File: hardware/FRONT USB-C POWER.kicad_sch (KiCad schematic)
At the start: 36 parts, among them Q3 PMPB11EN,115, Q4 PMPB11EN,115, Q5 PMPB11EN,115, Q6 PMPB11EN,115

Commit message: messing arround with pcb to finalise
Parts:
- added TP10, TP11: TestPoint, TestPoint:TestPoint_Pad_D1.5mm, symbol Connector:TestPoint
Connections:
- net B_USB-C_BUCK_OUT: now also TP10.1
- net F_USB-C_BUCK_OUT: now also TP11.1
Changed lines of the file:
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@@
   (junction (at 198.12 114.3) (diameter 0) (color 0 0 0 0)
   )
+  (junction (at 41.91 72.39) (diameter 0) (color 0 0 0 0)
+  )
   (junction (at 215.9 73.66) (diameter 0) (color 0 0 0 0)
   )
@@
   (junction (at 138.43 25.4) (diameter 0) (color 0 0 0 0)
   )
+  (junction (at 233.68 73.66) (diameter 0) (color 0 0 0 0)
+  )
   (junction (at 241.3 114.3) (diameter 0) (color 0 0 0 0)
   )
@@
     (stroke (width 0) (type default))
   )
+  (wire (pts (xy 41.91 72.39) (xy 44.45 72.39))
+    (stroke (width 0) (type default))
+  )
   (wire (pts (xy 215.9 73.66) (xy 219.71 73.66))
     (stroke (width 0) (type default))
@@
     (stroke (width 0) (type default))
   )
-  (wire (pts (xy 39.37 72.39) (xy 44.45 72.39))
-    (stroke (width 0) (type default))
-  )
-  (wire (pts (xy 228.6 73.66) (xy 237.49 73.66))
+  (wire (pts (xy 39.37 72.39) (xy 41.91 72.39))
+    (stroke (width 0) (type default))
+  )
+  (wire (pts (xy 228.6 73.66) (xy 233.68 73.66))
     (stroke (width 0) (type default))
   )
@@
   )
   (wire (pts (xy 104.14 87.63) (xy 96.52 87.63))
+    (stroke (width 0) (type default))
+  )
+  (wire (pts (xy 233.68 73.66) (xy 237.49 73.66))
     (stroke (width 0) (type default))
   )
@@
     )
   )
+  (symbol (lib_id "Connector:TestPoint") (at 41.91 72.39 0) (unit 1)
+    (in_bom yes) (on_board yes) (dnp no) (fields_autoplaced)
+    (property "Reference" "TP10" (at 43.307 68.4443 0)
+      (effects (font (size 1.27 1.27)) (justify left))
+    )
+    (property "Value" "TestPoint" (at 43.307 70.3653 0)
+      (effects (font (size 1.27 1.27)) (justify left))
+    )
+    (property "Footprint" "TestPoint:TestPoint_Pad_D1.5mm" (at 46.99 72.39 0)
+      (effects (font (size 1.27 1.27)) hide)
+    )
+    (property "Datasheet" "~" (at 46.99 72.39 0)
+      (effects (font (size 1.27 1.27)) hide)
+    )
+    (pin "1")
+    (instances
+      (project "usbc-car-module"
+        (path "/fae025e9-99c5-40c1-af6f-99dc1edbfa43/91b561d6-4186-4f6f-8a2c-57c2c305f210"
+          (reference "TP10") (unit 1)
+        )
+      )
+    )
+  )
   (symbol (lib_id "Device:C") (at 138.43 143.51 90) (unit 1)
     (in_bom yes) (on_board yes) (dnp no) (fields_autoplaced)
@@
         )
       )
+    )
+  )
+  (symbol (lib_id "Connector:TestPoint") (at 233.68 73.66 0) (unit 1)
+    (in_bom yes) (on_board yes) (dnp no) (fields_autoplaced)
+    (property "Reference" "TP11" (at 235.077 69.7143 0)
+      (effects (font (size 1.27 1.27)) (justify left))
+    )
+    (property "Value" "TestPoint" (at 235.077 71.6353 0)
+      (effects (font (size 1.27 1.27)) (justify left))
+    )
+    (property "Footprint" "TestPoint:TestPoint_Pad_D1.5mm" (at 238.76 73.66 0)
+      (effects (font (size 1.27 1.27)) hide)
+    )
+    (property "Datasheet" "~" (at 238.76 73.66 0)
+      (effects (font (size 1.27 1.27)) hide)
+    )
+    (pin "1")
+    (instances
+      (project "usbc-car-module"
+        (path "/fae025e9-99c5-40c1-af6f-99dc1edbfa43/91b561d6-4186-4f6f-8a2c-57c2c305f210"
+          (reference "TP11") (unit 1)
+        )
+      )

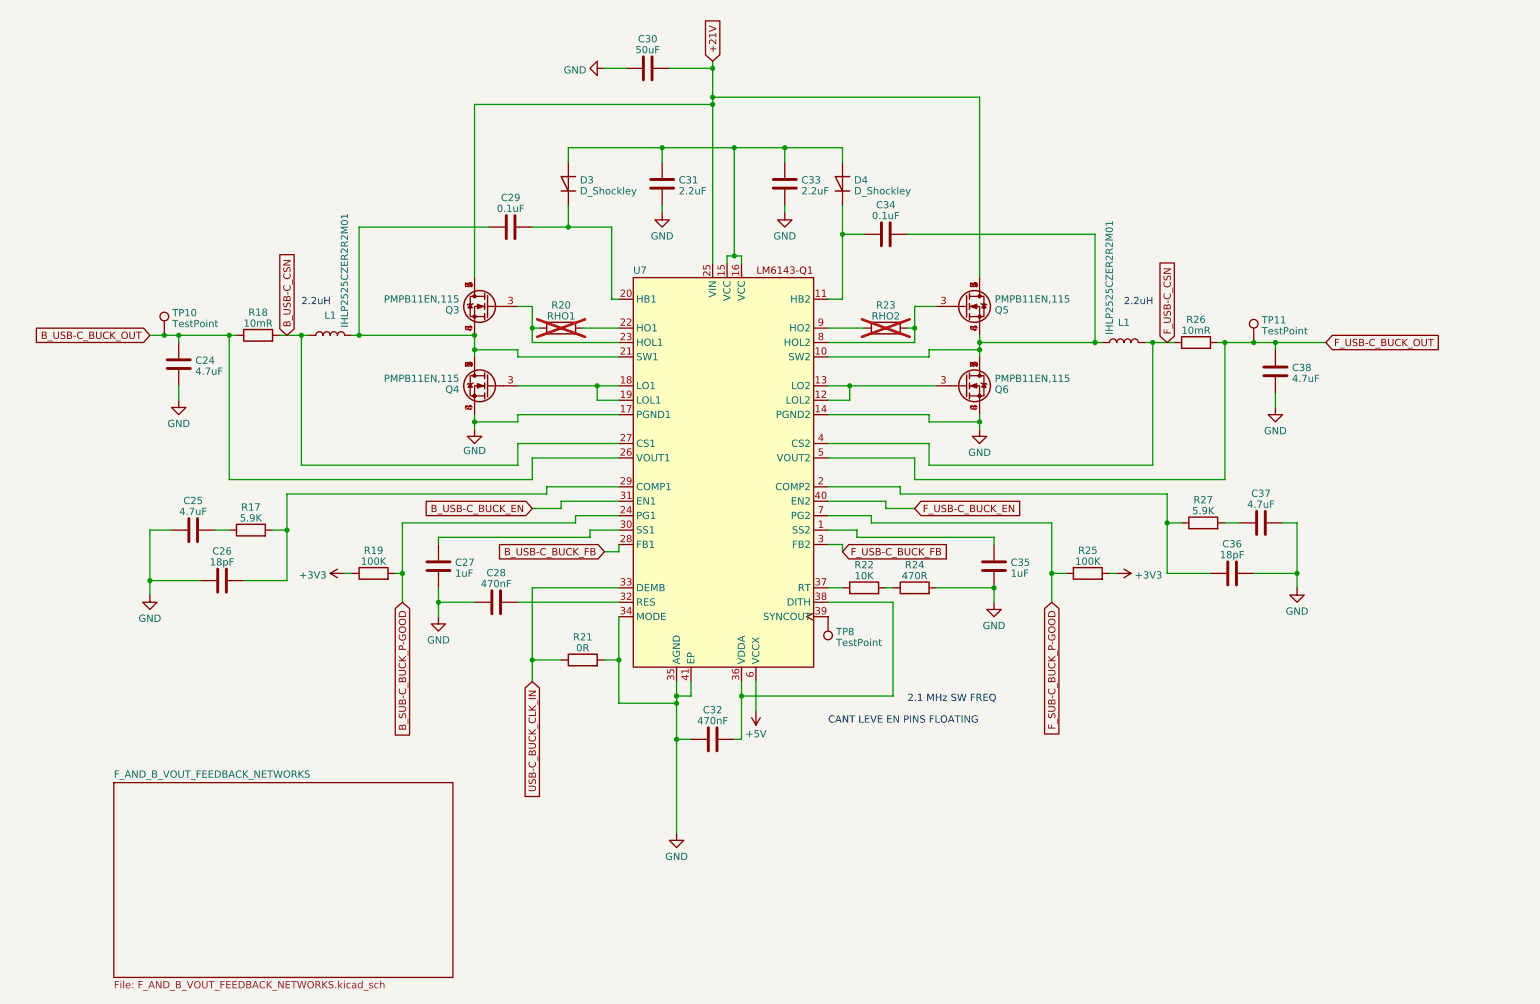
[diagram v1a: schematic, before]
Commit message: fixed DP issues and finneshed overall routeing
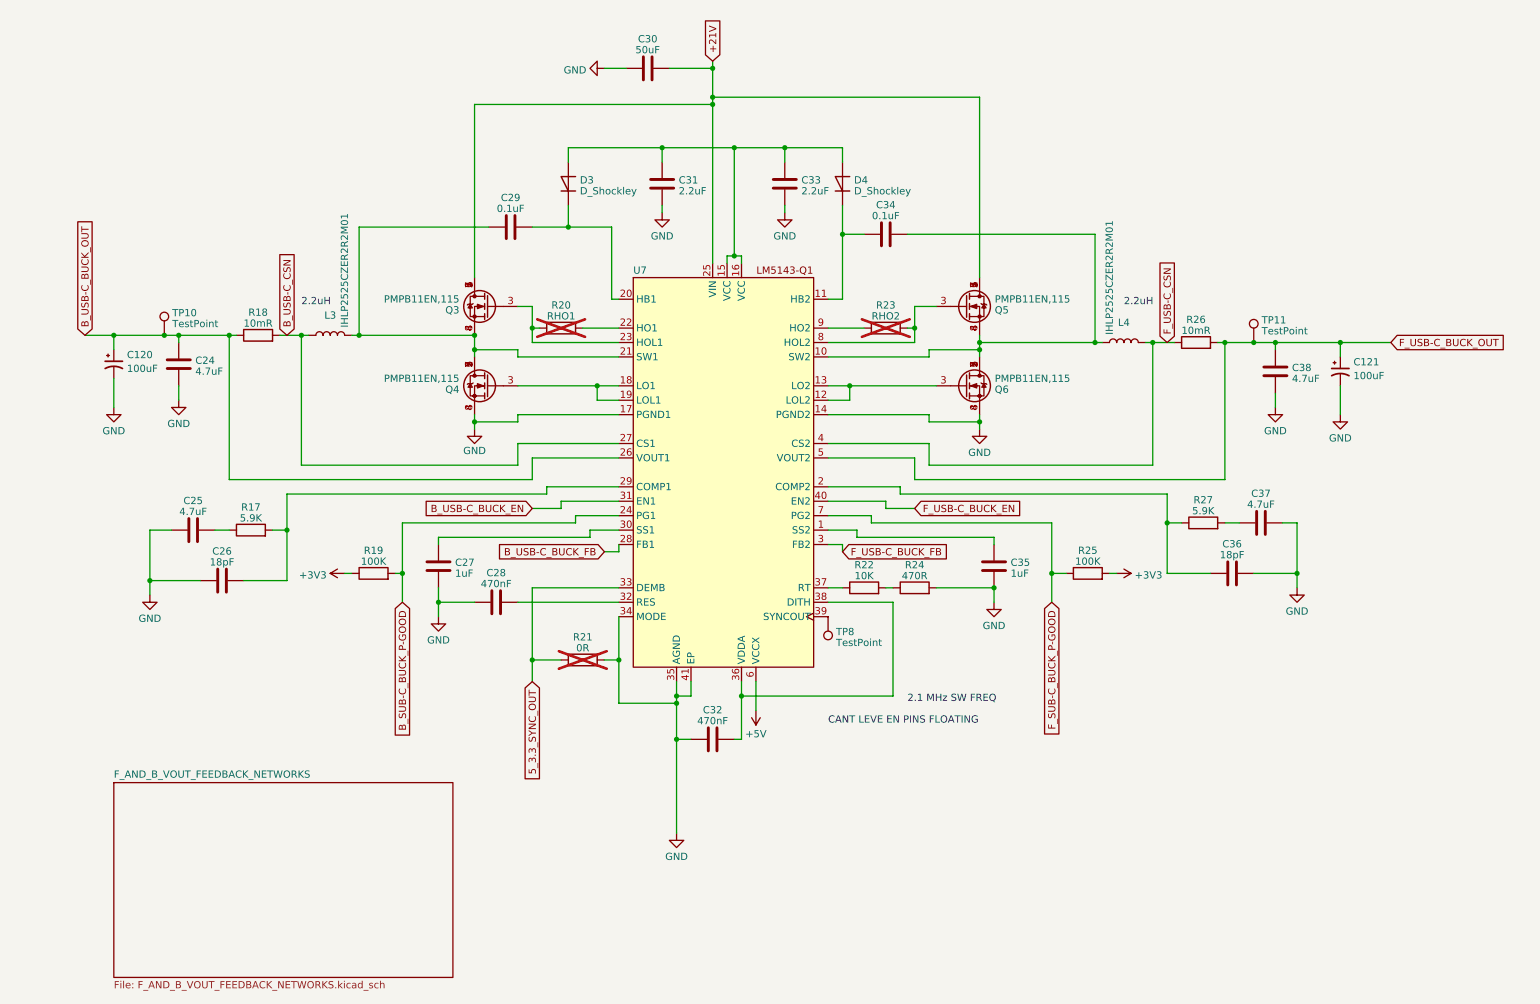
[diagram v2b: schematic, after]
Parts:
- added C120, C121: 100uF, Capacitor_SMD:CP_Elec_6.3x7.7, symbol Device:C_Polarized_Small_US
- R21: now not fitted
- renumbered L1 to L3, L1 to L4
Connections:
- net B_USB-C_BUCK_OUT: now also C120.1
- net F_USB-C_BUCK_OUT: now also C121.1
- net GND: now also C120.2, C121.2
- net USB-C_BUCK_CLK_IN renamed 5_3.3_SYNC_OUT
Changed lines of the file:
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@@
   (junction (at 198.12 114.3) (diameter 0) (color 0 0 0 0)
   )
+  (junction (at 248.92 73.66) (diameter 0) (color 0 0 0 0)
+  )
   (junction (at 41.91 72.39) (diameter 0) (color 0 0 0 0)
   )
@@
   (junction (at 44.45 72.39) (diameter 0) (color 0 0 0 0)
   )
+  (junction (at 33.02 72.39) (diameter 0) (color 0 0 0 0)
+  )
   (junction (at 106.68 71.12) (diameter 0) (color 0 0 0 0)
   )
@@
     (stroke (width 0) (type default))
   )
+  (wire (pts (xy 248.92 81.28) (xy 248.92 86.36))
+    (stroke (width 0) (type default))
+  )
   (wire (pts (xy 113.03 53.34) (xy 120.65 53.34))
     (stroke (width 0) (type default))
@@
     (stroke (width 0) (type default))
   )
+  (wire (pts (xy 33.02 72.39) (xy 33.02 74.93))
+    (stroke (width 0) (type default))
+  )
   (wire (pts (xy 158.75 116.84) (xy 161.29 116.84))
     (stroke (width 0) (type default))
@@
     (stroke (width 0) (type default))
   )
+  (wire (pts (xy 248.92 73.66) (xy 248.92 76.2))
+    (stroke (width 0) (type default))
+  )
   (wire (pts (xy 158.75 71.12) (xy 165.1 71.12))
     (stroke (width 0) (type default))
@@
     (stroke (width 0) (type default))
   )
+  (wire (pts (xy 248.92 73.66) (xy 257.81 73.66))
+    (stroke (width 0) (type default))
+  )
   (wire (pts (xy 138.43 25.4) (xy 138.43 30.48))
     (stroke (width 0) (type default))
@@
     (stroke (width 0) (type default))
   )
-  (wire (pts (xy 237.49 73.66) (xy 246.38 73.66))
+  (wire (pts (xy 237.49 73.66) (xy 248.92 73.66))
     (stroke (width 0) (type default))
   )
@@
     (stroke (width 0) (type default))
   )
+  (wire (pts (xy 33.02 80.01) (xy 33.02 85.09))
+    (stroke (width 0) (type default))
+  )
   (wire (pts (xy 173.99 67.31) (xy 177.8 67.31))
     (stroke (width 0) (type default))
@@
     (stroke (width 0) (type default))
   )
-  (wire (pts (xy 39.37 72.39) (xy 41.91 72.39))
+  (wire (pts (xy 27.94 72.39) (xy 33.02 72.39))
     (stroke (width 0) (type default))
   )
@@
   )
   (wire (pts (xy 158.75 86.36) (xy 176.53 86.36))
+    (stroke (width 0) (type default))
+  )
+  (wire (pts (xy 33.02 72.39) (xy 41.91 72.39))
     (stroke (width 0) (type default))
   )
@@
     )
   )
-  (global_label "B_USB-C_BUCK_OUT" (shape input) (at 39.37 72.39 180) (fields_autoplaced)
+  (global_label "5_3.3_SYNC_OUT" (shape input) (at 106.68 133.35 270) (fields_autoplaced)
     (effects (font (size 1.27 1.27)) (justify right))
-    (property "Intersheetrefs" "${INTERSHEET_REFS}" (at 12.1527 72.39 0)
+    (property "Intersheetrefs" "${INTERSHEET_REFS}" (at 106.68 151.9985 90)
       (effects (font (size 1.27 1.27)) (justify right) hide)
+    )
+  )
+  (global_label "B_USB-C_BUCK_OUT" (shape input) (at 27.94 72.39 90) (fields_autoplaced)
+    (effects (font (size 1.27 1.27)) (justify left))
+    (property "Intersheetrefs" "${INTERSHEET_REFS}" (at 27.94 49.8105 90)
+      (effects (font (size 1.27 1.27)) (justify left) hide)
     )
   )
@@
     )
   )
-  (global_label "USB-C_BUCK_CLK_IN" (shape input) (at 106.68 133.35 270) (fields_autoplaced)
-    (effects (font (size 1.27 1.27)) (justify right))
-    (property "Intersheetrefs" "${INTERSHEET_REFS}" (at 106.68 156.4549 90)
-      (effects (font (size 1.27 1.27)) (justify right) hide)
-    )
-  )
   (global_label "F_SUB-C_BUCK_P-GOOD" (shape input) (at 198.12 119.38 270) (fields_autoplaced)
     (effects (font (size 1.27 1.27)) (justify right))
@@
     )
   )
-  (global_label "F_USB-C_BUCK_OUT" (shape input) (at 246.38 73.66 0) (fields_autoplaced)
+  (global_label "F_USB-C_BUCK_OUT" (shape input) (at 257.81 73.66 0) (fields_autoplaced)
     (effects (font (size 1.27 1.27)) (justify left))
-    (property "Intersheetrefs" "${INTERSHEET_REFS}" (at 272.5087 73.66 0)
+    (property "Intersheetrefs" "${INTERSHEET_REFS}" (at 283.9387 73.66 0)
       (effects (font (size 1.27 1.27)) (justify left) hide)
     )
@@
         (path "/fae025e9-99c5-40c1-af6f-99dc1edbfa43/91b561d6-4186-4f6f-8a2c-57c2c305f210"
           (reference "#PWR029") (unit 1)
+        )
+      )
+    )
+  )
+  (symbol (lib_id "Device:C_Polarized_Small_US") (at 33.02 77.47 0) (unit 1)
+    (in_bom yes) (on_board yes) (dnp no) (fields_autoplaced)
+    (property "Reference" "C120" (at 35.3314 75.8261 0)
+      (effects (font (size 1.27 1.27)) (justify left))
+    )
+    (property "Value" "100uF" (at 35.3314 78.2503 0)
+      (effects (font (size 1.27 1.27)) (justify left))
+    )
+    (property "Footprint" "Capacitor_SMD:CP_Elec_6.3x7.7" (at 33.02 77.47 0)
+      (effects (font (size 1.27 1.27)) hide)
+    )
+    (property "Datasheet" "~" (at 33.02 77.47 0)
+      (effects (font (size 1.27 1.27)) hide)
+    )
+    (pin "1")
+    (pin "2")
+    (instances
+      (project "usbc-car-module"
+        (path "/fae025e9-99c5-40c1-af6f-99dc1edbfa43/91b561d6-4186-4f6f-8a2c-57c2c305f210"
+          (reference "C120") (unit 1)
         )
       )
@@
   )
   (symbol (lib_id "Device:R") (at 115.57 129.54 90) (unit 1)
-    (in_bom yes) (on_board yes) (dnp no) (fields_autoplaced)
+    (in_bom yes) (on_board yes) (dnp yes) (fields_autoplaced)
     (property "Reference" "R21" (at 115.57 125.5141 90)
       (effects (font (size 1.27 1.27)))
@@
         (path "/fae025e9-99c5-40c1-af6f-99dc1edbfa43/91b561d6-4186-4f6f-8a2c-57c2c305f210"
           (reference "TP8") (unit 1)
+        )
+      )
+    )
+  )
+  (symbol (lib_id "Device:C_Polarized_Small_US") (at 248.92 78.74 0) (unit 1)
+    (in_bom yes) (on_board yes) (dnp no) (fields_autoplaced)
+    (property "Reference" "C121" (at 251.2314 77.0961 0)
+      (effects (font (size 1.27 1.27)) (justify left))
+    )
+    (property "Value" "100uF" (at 251.2314 79.5203 0)
+      (effects (font (size 1.27 1.27)) (justify left))
+    )
+    (property "Footprint" "Capacitor_SMD:CP_Elec_6.3x7.7" (at 248.92 78.74 0)
+      (effects (font (size 1.27 1.27)) hide)
+    )
+    (property "Datasheet" "~" (at 248.92 78.74 0)
+      (effects (font (size 1.27 1.27)) hide)
+    )
+    (pin "1")
+    (pin "2")
+    (instances
+      (project "usbc-car-module"
+        (path "/fae025e9-99c5-40c1-af6f-99dc1edbfa43/91b561d6-4186-4f6f-8a2c-57c2c305f210"
+          (reference "C121") (unit 1)
         )
       )
@@
   (symbol (lib_id "Device:L") (at 210.82 73.66 90) (unit 1)
     (in_bom yes) (on_board yes) (dnp no)
-    (property "Reference" "L1" (at 210.82 70.1447 90)
+    (property "Reference" "L4" (at 210.82 70.1447 90)
       (effects (font (size 1.27 1.27)))
     )
@@
     (instances
       (project "usbc-car-module"
-        (path "/fae025e9-99c5-40c1-af6f-99dc1edbfa43/d2e16279-165c-4434-90cd-263b76553257"
-          (reference "L1") (unit 1)
-        )
         (path "/fae025e9-99c5-40c1-af6f-99dc1edbfa43/91b561d6-4186-4f6f-8a2c-57c2c305f210"
           (reference "L4") (unit 1)
@@
         (path "/fae025e9-99c5-40c1-af6f-99dc1edbfa43/91b561d6-4186-4f6f-8a2c-57c2c305f210"
           (reference "R24") (unit 1)
+        )
+      )
+    )
+  )
+  (symbol (lib_id "power:GND") (at 33.02 85.09 0) (unit 1)
+    (in_bom yes) (on_board yes) (dnp no) (fields_autoplaced)
+    (property "Reference" "#PWR0158" (at 33.02 91.44 0)
+      (effects (font (size 1.27 1.27)) hide)
+    )
+    (property "Value" "GND" (at 33.02 89.2255 0)
+      (effects (font (size 1.27 1.27)))
+    )
+    (property "Footprint" "" (at 33.02 85.09 0)
+      (effects (font (size 1.27 1.27)) hide)
+    )
+    (property "Datasheet" "" (at 33.02 85.09 0)
+      (effects (font (size 1.27 1.27)) hide)
+    )
+    (pin "1")
+    (instances
+      (project "usbc-car-module"
+        (path "/fae025e9-99c5-40c1-af6f-99dc1edbfa43/91b561d6-4186-4f6f-8a2c-57c2c305f210"
+          (reference "#PWR0158") (unit 1)
         )
       )
@@
     )
   )
+  (symbol (lib_id "power:GND") (at 248.92 86.36 0) (unit 1)
+    (in_bom yes) (on_board yes) (dnp no) (fields_autoplaced)
+    (property "Reference" "#PWR0159" (at 248.92 92.71 0)
+      (effects (font (size 1.27 1.27)) hide)
+    )
+    (property "Value" "GND" (at 248.92 90.4955 0)
+      (effects (font (size 1.27 1.27)))
+    )
+    (property "Footprint" "" (at 248.92 86.36 0)
+      (effects (font (size 1.27 1.27)) hide)
+    )
+    (property "Datasheet" "" (at 248.92 86.36 0)
+      (effects (font (size 1.27 1.27)) hide)
+    )
+    (pin "1")
+    (instances
+      (project "usbc-car-module"
+        (path "/fae025e9-99c5-40c1-af6f-99dc1edbfa43/91b561d6-4186-4f6f-8a2c-57c2c305f210"
+          (reference "#PWR0159") (unit 1)
+        )
+      )
+    )
+  )
   (symbol (lib_id "power:GND") (at 187.96 119.38 0) (unit 1)
     (in_bom yes) (on_board yes) (dnp no) (fields_autoplaced)
@@
   (symbol (lib_id "Device:L") (at 71.12 72.39 90) (unit 1)
     (in_bom yes) (on_board yes) (dnp no)
-    (property "Reference" "L1" (at 71.12 68.8747 90)
+    (property "Reference" "L3" (at 71.12 68.8747 90)
       (effects (font (size 1.27 1.27)))
     )
@@
     (instances
       (project "usbc-car-module"
-        (path "/fae025e9-99c5-40c1-af6f-99dc1edbfa43/d2e16279-165c-4434-90cd-263b76553257"
-          (reference "L1") (unit 1)
-        )
         (path "/fae025e9-99c5-40c1-af6f-99dc1edbfa43/91b561d6-4186-4f6f-8a2c-57c2c305f210"
           (reference "L3") (unit 1)

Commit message: minor revisions
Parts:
- D3, D4: footprint Diode_SMD:D_SMA -> Diode_SMD:D_SOD-523
- U7: value ~ -> LM5143
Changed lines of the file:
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@@
       (effects (font (size 1.27 1.27)) (justify left))
     )
-    (property "Value" "~" (at 149.86 76.2 0)
+    (property "Value" "LM5143" (at 149.86 76.2 0)
       (effects (font (size 1.27 1.27)))
     )
@@
       (effects (font (size 1.27 1.27)) (justify right))
     )
-    (property "Footprint" "Diode_SMD:D_SMA" (at 161.29 45.72 0)
+    (property "Footprint" "Diode_SMD:D_SOD-523" (at 161.29 45.72 0)
       (effects (font (size 1.27 1.27)) hide)
     )
@@
       (effects (font (size 1.27 1.27)) (justify right))
     )
-    (property "Footprint" "Diode_SMD:D_SMA" (at 113.03 45.72 0)
-      (effects (font (size 1.27 1.27)) hide)
-    )
+    (property "Footprint" "Diode_SMD:D_SOD-523" (at 113.03 45.72 0)
+      (effects (font (size 1.27 1.27)) hide)
+    )
